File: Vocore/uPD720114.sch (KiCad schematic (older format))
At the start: 61 parts, among them U10 DLW21SN900SQ2, U13 IP4220CZ6, U14 IP4220CZ6, U15 AP2146, U16 AP2146, U2 DLW21SN900SQ2, U3 IP4220CZ6, U4 UPD720114-QFP48, U5 USB-AF-90, U9 DLW21SN900SQ2, X1 30MHz

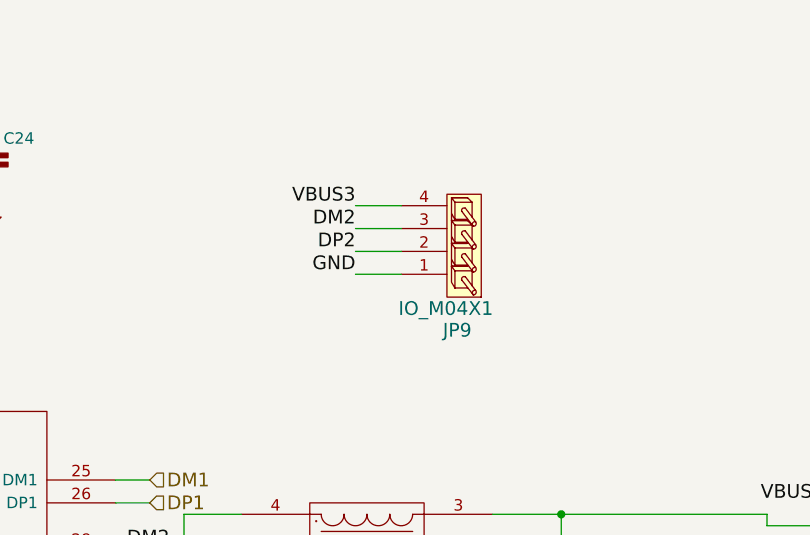
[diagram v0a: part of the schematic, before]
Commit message: Vocore第二版修改完成
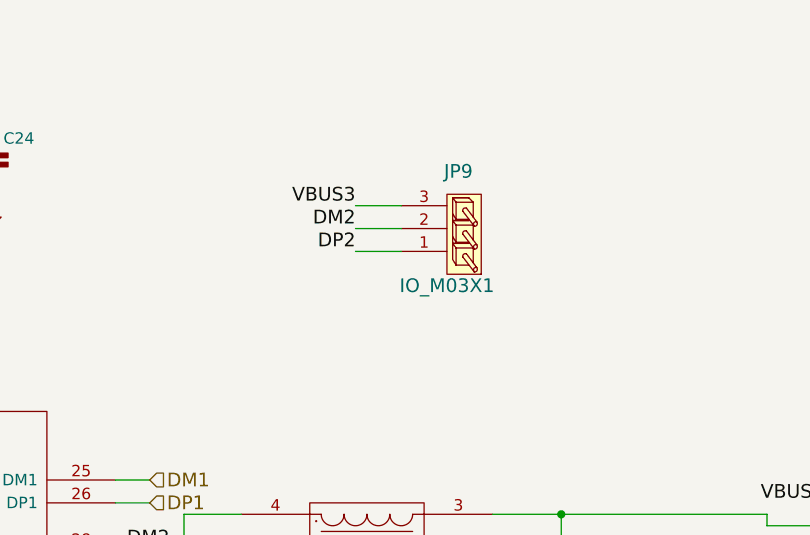
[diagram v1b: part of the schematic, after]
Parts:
- removed JP9: IO_M04X1, IO_M04X1, symbol IO_M04X1
- added JP9: IO_M03X1, IO_M03X1, symbol IO_M03X1
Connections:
- net DM2: now also JP9.2
- net DP2: now also JP9.1
- net VBUS3: now also JP9.3
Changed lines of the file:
@@
-EESchema Schematic File Version 2  date 2014/12/30 17:54:50
+EESchema Schematic File Version 2  date 2015/1/14 16:22:56
 LIBS:C
 LIBS:IC
@@
 LIBS:rcl
 LIBS:gl
+LIBS:ATMEGA32U4-cache
+LIBS:uPD720114-cache
+LIBS:vc-cache
+LIBS:vocore-cache
+LIBS:SchumyHao
 LIBS:vocore-cache
 EELAYER 27 0
@@
 Sheet 2 3
 Title ""
-Date "30 dec 2014"
+Date "14 jan 2015"
 Rev ""
 Comp ""
@@
 Text Label 6250 1700 2    60   ~ 0
 DP2
-Text Label 6250 1800 2    60   ~ 0
-GND
-$Comp
-L IO_M04X1 JP9
-U 1 1 549C186C
-P 6700 1550
-F 0 "JP9" H 6705 2045 60  0000 C CNN
-F 1 "IO_M04X1" H 6755 1950 60  0000 C CNN
-F 2 "IO_M04X1" H 6765 1300 60  0001 C CNN
-F 3 "~" H 6700 1550 60  0000 C CNN
-	1    6700 1550
+Wire Wire Line
+	6250 1500 6450 1500
+Wire Wire Line
+	6250 1600 6450 1600
+Wire Wire Line
+	6250 1700 6450 1700
+$Comp
+L IO_M03X1 JP9
+U 1 1 54B4B18C
+P 6700 1600
+F 0 "JP9" H 6700 1350 60  0000 C CNN
+F 1 "IO_M03X1" H 6750 1850 60  0000 C CNN
+F 2 "IO_M03X1" H 6760 1255 60  0001 C CNN
+F 3 "~" H 6700 1600 60  0000 C CNN
+	1    6700 1600
 	-1   0    0    1
 $EndComp
-Wire Wire Line
-	6250 1500 6450 1500
-Wire Wire Line
-	6250 1600 6450 1600
-Wire Wire Line
-	6250 1700 6450 1700
-Wire Wire Line
-	6250 1800 6450 1800
 $EndSCHEMATC
